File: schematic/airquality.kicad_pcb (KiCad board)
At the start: 4 copper layers, 40 x 98 mm, 55 parts, among them J1 TYPE-C-31-M-12, Q1 BC817, Q2 BC817, U1 ESP32-WROOM-32D, U2 BME280, U3 SN74LV1T34DCK, U4 SGP30, U5 TLV70218_SOT23-5, U6 PMS7003, U7 AMS1117-3.3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

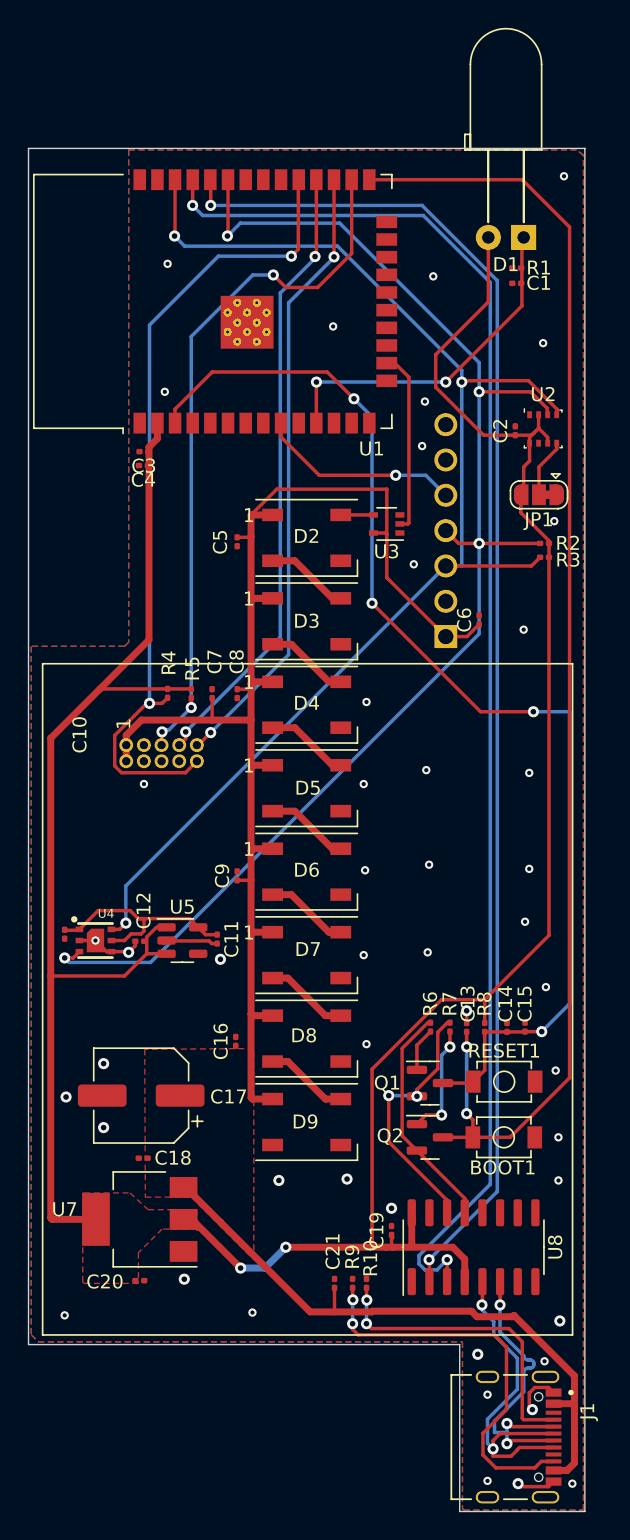
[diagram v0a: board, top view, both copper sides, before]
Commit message: Fix orientation of particulate sensor
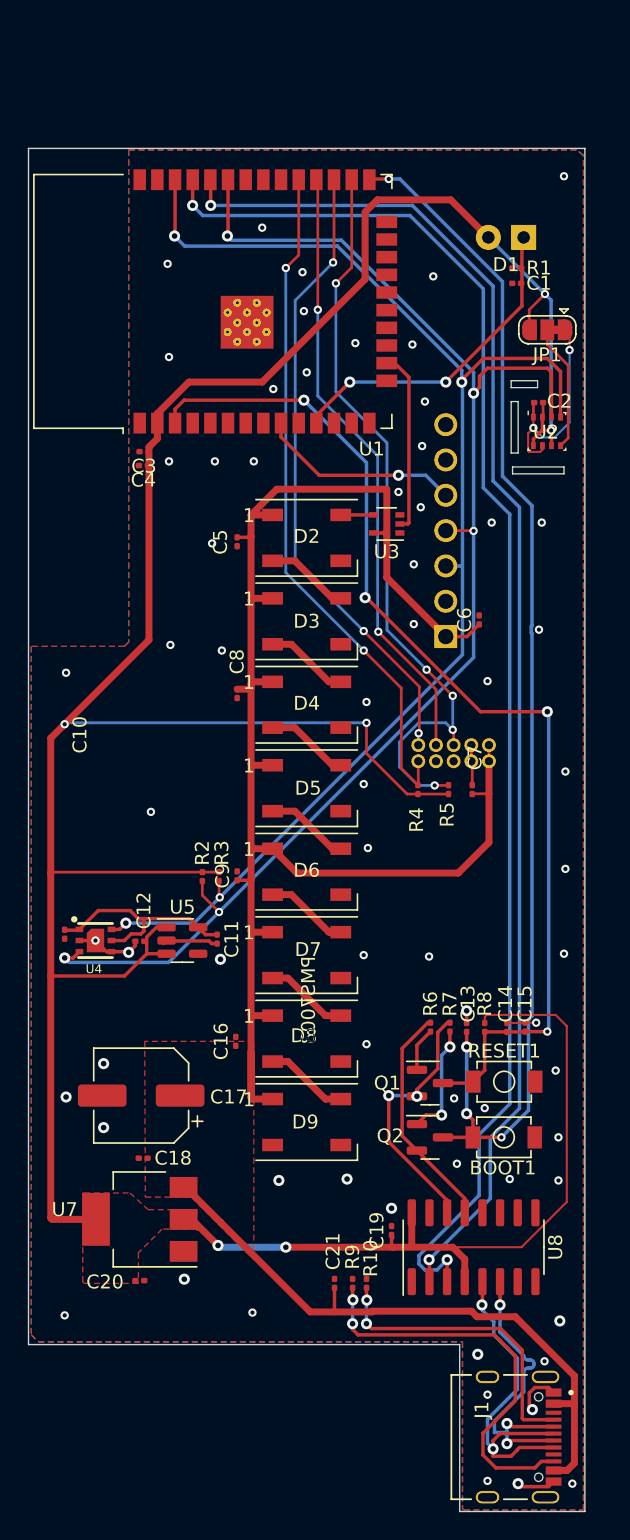
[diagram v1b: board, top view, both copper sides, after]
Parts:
- U6: moved to B.Cu
- moved R2 34.3 mm to (78.5, 98.4), turned to -90 degrees
- moved R3 32.8 mm to (79.7, 98.4), turned to -90 degrees
- moved C7 19.9 mm to (97.9, 92.1)
- moved R5 19.7 mm to (96.2, 92.1), turned to 90 degrees
- moved R4 19.3 mm to (94.0, 92.1), turned to 90 degrees
- moved JP1 11.9 mm to (103.3, 59.0)
- moved C2 2.63 mm to (102.7, 64.3), turned to 180 degrees
- moved U2 0.33 mm to (103.3, 66.3)
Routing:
- net +3V3: track 202.6 -> 231.6 mm, vias 2 -> 6
- net GND: track 15.9 -> 35.3 mm, vias 48 -> 69
- net VBUS: track 145.5 -> 157.9 mm
- net PMS_SET: track 58.7 -> 49.4 mm
- net ESP_IO0: track 95.6 -> 87.9 mm, vias 2 -> 4
- net ESP_EN: track 82.3 -> 76.7 mm
- net Net-(JP1-C): track 4.23 -> 9.18 mm
- net PMS_RESET: track 51.2 -> 55.1 mm, vias 3 -> 5
- net Iluminance: track 25.0 -> 22.8 mm
- net ESP_RX: track 98.7 -> 99.6 mm
- net SCL: track 95.6 -> 96.5 mm, vias 3 -> 4
- net PMS_TX: track 44.7 -> 45.5 mm, vias 2 -> 3
- net SDA: track 100.2 -> 101.0 mm, vias 4 -> 5
- net PMS_RX: track 44.7 -> 44.1 mm
- net ESP_TX: track 102.3 -> 102.9 mm
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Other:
- outline, holes or cut-outs redrawn
- copper layers 4 -> 2

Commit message: cleanup
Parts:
- moved C19 0.30 mm to (91.8, 123.8)
- moved C20 0.10 mm to (74.0, 127.3)
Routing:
- net VBUS: track 157.9 -> 151.7 mm
- net GND: track 35.3 -> 30.6 mm, vias 69 -> 80
- net PMS_RESET: track 55.1 -> 55.7 mm, vias 5 -> 4
